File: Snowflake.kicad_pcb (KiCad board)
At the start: 2 copper layers, 168.4 x 106 mm, 34 parts, among them J1 , J2 

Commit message: updated
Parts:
- removed the ? at (217.1, 108.1)
- added ?: , Big pad, F.Cu at (237.6, 117.9)
- added ?: , Big pad, F.Cu at (224.5, 95.4)
- added ?: , Big pad, F.Cu at (235.6, 95.2)
- added ?: , Big pad, F.Cu at (222.6, 117.7)
- added ?: , Big pad, F.Cu at (243.1, 105.9)
- added ?: , Big pad, F.Cu at (222.1, 117.5)
- 2: renamed from LED5; value WS2812B -> (none)
- 4: renamed from LED3; value WS2812B -> (none)
- 5: renamed from LED2; value WS2812B -> (none)
- 6: renamed from LED104; value WS2812B -> (none)
- 7: renamed from LED101; value WS2812B -> (none)
- 8: renamed from LED102; value WS2812B -> (none)
- 9: renamed from LED103; value WS2812B -> (none)
- ?: renamed from LED7; value WS2812B -> (none)
- moved 4 2.41 mm to (124.3, 84.1)
- moved 8 1.25 mm to (123.8, 129.7)
- moved 5 1.20 mm to (109.6, 58.8)
- moved J1 0.88 mm to (230.1, 112.0)
- moved ? 0.51 mm to (217.1, 106.0)
- moved 9 0.23 mm to (109.1, 155.1)
- renumbered LED6 to 1, LED4 to 3, J2 to ?
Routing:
- net /DIN: track 66.7 -> 79.6 mm
- net /DOUT: track 179.3 -> 187.0 mm
- net /VCC: track 379.7 -> 384.3 mm, vias 22 -> 21
- net /GND: track 343.0 -> 347.2 mm
- net Net-(LED2-Pad4): track 21.6 -> 25.2 mm
- net Net-(LED3-Pad4): track 31.9 -> 29.5 mm
- net (no net): track 0.00 -> 1.97 mm, vias 0 -> 2
- net Net-(LED102-Pad2): track 23.3 -> 24.8 mm
- net Net-(LED101-Pad2): track 65.2 -> 63.9 mm
- net Net-(LED104-Pad4): track 65.9 -> 66.9 mm
- net Net-(LED6-Pad4): track 28.1 -> 29.1 mm
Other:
- board text added: "1"
- board text added: "2"
- board text added: "3"
- board text added: "4"
- board text added: "5"
- board text added: "6"
- board text added: "V0.9 Snowflake"
- board text added: "eag"

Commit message: updated
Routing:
- net (no net): track 1.97 -> 5.84 mm, vias 2 -> 3
- net /GND: track 347.2 -> 345.5 mm
- net /VCC: track 384.3 -> 385.9 mm, vias 21 -> 22
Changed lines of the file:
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@@
     (thickness 1.6)
     (drawings 92)
-    (tracks 287)
+    (tracks 293)
     (zones 0)
     (modules 39)
@@
   )
   (setup
-    (last_trace_width 0.25)
+    (last_trace_width 2)
     (user_trace_width 0.5)
     (user_trace_width 1)
@@
   (gr_line (start 139.085367 110.601745) (end 110.515198 160.077503) (layer Edge.Cuts) (width 0.1))
   (gr_line (start 131.016096 110.601745) (end 139.085367 110.601745) (layer Edge.Cuts) (width 0.1))
+  (segment (start 243.0145 105.664) (end 239.141 105.664) (width 2) (layer F.Cu) (net 0) (status 400000))
+  (via (at 239.141 105.664) (size 0.6) (drill 0.4) (layers F.Cu B.Cu) (net 0))
   (segment (start 235.290295 119.016015) (end 233.3625 118.9355) (width 2) (layer F.Cu) (net 0))
   (via (at 233.3625 118.9355) (size 0.6) (drill 0.4) (layers F.Cu B.Cu) (net 0))
@@
   (via (at 233.372871 118.953707) (size 0.6) (drill 0.4) (layers F.Cu B.Cu) (net 0))
   (segment (start 233.372871 118.953707) (end 233.3625 118.9355) (width 2) (layer F.Cu) (net 0))
+  (segment (start 239.395 98.8695) (end 240.8555 99.568) (width 2) (layer F.Cu) (net 1))
+  (via (at 240.8555 99.568) (size 0.6) (drill 0.4) (layers F.Cu B.Cu) (net 1))
+  (segment (start 240.8555 99.568) (end 240.862326 99.556012) (width 2) (layer B.Cu) (net 1))
   (segment (start 222.28403 117.711985) (end 221.361 115.951) (width 2) (layer F.Cu) (net 1))
   (via (at 221.361 115.951) (size 0.6) (drill 0.4) (layers F.Cu B.Cu) (net 1))
@@
   (segment (start 235.077 117.983) (end 241.935 114.1095) (width 2) (layer B.Cu) (net 1))
   (segment (start 241.935 114.1095) (end 241.935 108.585) (width 2) (layer B.Cu) (net 1))
-  (segment (start 241.9985 100.203) (end 239.459092 98.756948) (width 2) (layer B.Cu) (net 1))
+  (segment (start 241.9985 100.203) (end 240.862326 99.556012) (width 2) (layer B.Cu) (net 1))
+  (segment (start 240.862326 99.556012) (end 239.459092 98.756948) (width 2) (layer B.Cu) (net 1))
   (segment (start 239.459092 98.756948) (end 238.288953 98.090619) (width 2) (layer B.Cu) (net 1))
   (segment (start 238.288953 98.090619) (end 237.4265 97.5995) (width 2) (layer B.Cu) (net 1))
@@
   (segment (start 166.9415 105.41) (end 136.271 105.41) (width 2) (layer B.Cu) (net 1))
   (segment (start 136.271 105.41) (end 133.985 105.41) (width 2) (layer B.Cu) (net 1))
-  (segment (start 224.663 119.126) (end 226.633966 115.698233) (width 2) (layer B.Cu) (net 2))
-  (via (at 226.633966 115.698233) (size 0.6) (drill 0.4) (layers F.Cu B.Cu) (net 2))
-  (segment (start 226.633966 115.698233) (end 226.6315 115.697) (width 2) (layer F.Cu) (net 2))
-  (segment (start 237.70997 117.619015) (end 235.6485 114.173) (width 2) (layer F.Cu) (net 2))
-  (via (at 235.6485 114.173) (size 0.6) (drill 0.4) (layers F.Cu B.Cu) (net 2))
-  (segment (start 235.30153 95.169485) (end 233.3625 98.4885) (width 2) (layer F.Cu) (net 2))
-  (via (at 233.3625 98.4885) (size 0.6) (drill 0.4) (layers F.Cu B.Cu) (net 2))
-  (segment (start 233.3625 98.4885) (end 233.338283 98.532759) (width 2) (layer B.Cu) (net 2))
-  (segment (start 222.272795 96.537015) (end 224.409 100.1395) (width 2) (layer F.Cu) (net 2))
-  (via (at 224.409 100.1395) (size 0.6) (drill 0.4) (layers F.Cu B.Cu) (net 2))
-  (segment (start 224.409 100.1395) (end 224.189382 100.281244) (width 2) (layer B.Cu) (net 2))
-  (segment (start 243.0145 105.664) (end 238.887 105.664) (width 2) (layer F.Cu) (net 2))
-  (via (at 238.887 105.664) (size 0.6) (drill 0.4) (layers F.Cu B.Cu) (net 2))
-  (segment (start 238.887 105.664) (end 238.8235 105.664) (width 2) (layer B.Cu) (net 2))
+  (segment (start 239.2045 107.188) (end 239.141 108.6485) (width 2) (layer F.Cu) (net 2))
+  (via (at 239.141 108.6485) (size 0.6) (drill 0.4) (layers F.Cu B.Cu) (net 2))
+  (segment (start 235.458 107.188) (end 239.2045 107.188) (width 2) (layer F.Cu) (net 2) (status 400000))
+  (via (at 239.2045 107.188) (size 0.6) (drill 0.4) (layers F.Cu B.Cu) (net 2))
+  (segment (start 239.2045 107.188) (end 239.141 107.188) (width 2) (layer B.Cu) (net 2))
+  (segment (start 224.663 119.126) (end 226.6315 115.697) (width 2) (layer B.Cu) (net 2))
+  (via (at 226.6315 115.697) (size 0.6) (drill 0.4) (layers F.Cu B.Cu) (net 2))
+  (segment (start 226.6315 115.697) (end 226.629034 115.695767) (width 2) (layer F.Cu) (net 2))
+  (segment (start 237.70997 117.619015) (end 236.0295 114.173) (width 2) (layer F.Cu) (net 2) (status 400000))
+  (via (at 236.0295 114.173) (size 0.6) (drill 0.4) (layers F.Cu B.Cu) (net 2))
+  (segment (start 235.30153 95.169485) (end 233.553 98.425) (width 2) (layer F.Cu) (net 2) (status 400000))
+  (via (at 233.553 98.425) (size 0.6) (drill 0.4) (layers F.Cu B.Cu) (net 2))
+  (segment (start 233.553 98.425) (end 233.528783 98.469259) (width 2) (layer B.Cu) (net 2))
+  (segment (start 222.272795 96.537015) (end 224.282 99.822) (width 2) (layer F.Cu) (net 2) (status 400000))
+  (via (at 224.282 99.822) (size 0.6) (drill 0.4) (layers F.Cu B.Cu) (net 2))
+  (segment (start 224.282 99.822) (end 224.062382 99.963744) (width 2) (layer B.Cu) (net 2))
   (via (at 213.614 108.5215) (size 0.6) (drill 0.4) (layers F.Cu B.Cu) (net 2))
   (segment (start 213.614 108.5215) (end 216.9795 108.5215) (width 2) (layer F.Cu) (net 2))
@@
   (segment (start 211.2645 107.95) (end 213.614 108.5215) (width 2) (layer B.Cu) (net 2))
   (segment (start 220.98 108.3945) (end 220.98 108.0135) (width 2) (layer B.Cu) (net 2))
-  (segment (start 226.6315 115.697) (end 227.3935 116.078) (width 2) (layer B.Cu) (net 2))
+  (segment (start 226.629034 115.695767) (end 227.391034 116.076767) (width 2) (layer B.Cu) (net 2))
   (segment (start 173.85 108.457) (end 175.7045 108.1405) (width 1) (layer F.Cu) (net 2))
   (via (at 175.7045 108.1405) (size 0.6) (drill 0.4) (layers F.Cu B.Cu) (net 2))
@@
   (segment (start 131.495605 99.590527) (end 131.3815 103.5685) (width 2) (layer F.Cu) (net 2))
   (segment (start 131.3815 103.5685) (end 131.38138 108.188374) (width 2) (layer F.Cu) (net 2))
-  (segment (start 227.3935 116.078) (end 227.401315 116.064323) (width 2) (layer B.Cu) (net 2))
+  (segment (start 227.391034 116.076767) (end 227.398849 116.06309) (width 2) (layer B.Cu) (net 2))
   (segment (start 134.493 107.95) (end 134.492778 108.052098) (width 2) (layer B.Cu) (net 2))
   (via (at 134.493 107.95) (size 0.6) (drill 0.4) (layers F.Cu B.Cu) (net 2))
@@
   (segment (start 235.458 107.188) (end 233.426 107.188) (width 1) (layer F.Cu) (net 2))
   (segment (start 233.426 107.188) (end 232.27 108.33) (width 1) (layer F.Cu) (net 2))
-  (segment (start 235.458 107.188) (end 238.76 107.188) (width 2) (layer F.Cu) (net 2))
-  (via (at 238.76 107.188) (size 0.6) (drill 0.4) (layers F.Cu B.Cu) (net 2))
-  (segment (start 220.98 102.235) (end 224.570382 100.090744) (width 2) (layer B.Cu) (net 2))
-  (segment (start 224.570382 100.090744) (end 230.124 96.774) (width 2) (layer B.Cu) (net 2))
+  (segment (start 220.98 101.727) (end 224.443382 99.773244) (width 2) (layer B.Cu) (net 2))
+  (segment (start 224.443382 99.773244) (end 230.1875 96.5835) (width 2) (layer B.Cu) (net 2))
   (segment (start 220.98 112.395) (end 220.98 108.0135) (width 2) (layer B.Cu) (net 2))
-  (segment (start 220.98 108.0135) (end 220.98 102.235) (width 2) (layer B.Cu) (net 2))
-  (segment (start 229.87 117.475) (end 227.401315 116.064323) (width 2) (layer B.Cu) (net 2))
-  (segment (start 227.401315 116.064323) (end 220.98 112.395) (width 2) (layer B.Cu) (net 2))
-  (segment (start 238.76 112.395) (end 235.6485 114.173) (width 2) (layer B.Cu) (net 2))
-  (segment (start 235.6485 114.173) (end 229.87 117.475) (width 2) (layer B.Cu) (net 2))
-  (segment (start 238.76 101.6) (end 238.8235 105.664) (width 2) (layer B.Cu) (net 2))
-  (segment (start 238.8235 105.664) (end 238.8235 106.3625) (width 2) (layer B.Cu) (net 2))
-  (segment (start 238.8235 106.3625) (end 238.76 107.188) (width 2) (layer B.Cu) (net 2))
-  (segment (start 238.76 107.188) (end 238.76 112.395) (width 2) (layer B.Cu) (net 2))
-  (segment (start 230.124 96.774) (end 233.338283 98.532759) (width 2) (layer B.Cu) (net 2))
-  (segment (start 233.338283 98.532759) (end 233.4895 98.6155) (width 2) (layer B.Cu) (net 2))
-  (segment (start 233.4895 98.6155) (end 233.619012 98.687874) (width 2) (layer B.Cu) (net 2))
-  (segment (start 233.619012 98.687874) (end 238.76 101.6) (width 2) (layer B.Cu) (net 2))
+  (segment (start 220.98 108.0135) (end 220.98 101.727) (width 2) (layer B.Cu) (net 2))
+  (segment (start 230.124 117.602) (end 227.398849 116.06309) (width 2) (layer B.Cu) (net 2))
+  (segment (start 227.398849 116.06309) (end 220.98 112.395) (width 2) (layer B.Cu) (net 2))
+  (segment (start 239.141 112.395) (end 236.0295 114.173) (width 2) (layer B.Cu) (net 2))
+  (segment (start 236.0295 114.173) (end 230.124 117.602) (width 2) (layer B.Cu) (net 2))
+  (segment (start 239.141 101.7905) (end 239.141 105.664) (width 2) (layer B.Cu) (net 2))
+  (segment (start 239.141 105.664) (end 239.141 107.188) (width 2) (layer B.Cu) (net 2))
+  (segment (start 239.141 107.188) (end 239.141 108.6485) (width 2) (layer B.Cu) (net 2))
+  (segment (start 239.141 108.6485) (end 239.141 112.395) (width 2) (layer B.Cu) (net 2))
+  (segment (start 230.1875 96.5835) (end 233.528783 98.469259) (width 2) (layer B.Cu) (net 2))
+  (segment (start 233.528783 98.469259) (end 233.68 98.552) (width 2) (layer B.Cu) (net 2))
+  (segment (start 233.68 98.552) (end 233.809512 98.624374) (width 2) (layer B.Cu) (net 2))
+  (segment (start 233.809512 98.624374) (end 239.141 101.7905) (width 2) (layer B.Cu) (net 2))
   (segment (start 203.06 108.33) (end 205.486 107.95) (width 1) (layer F.Cu) (net 2))
   (via (at 205.486 107.95) (size 0.6) (drill 0.4) (layers F.Cu B.Cu) (net 2))

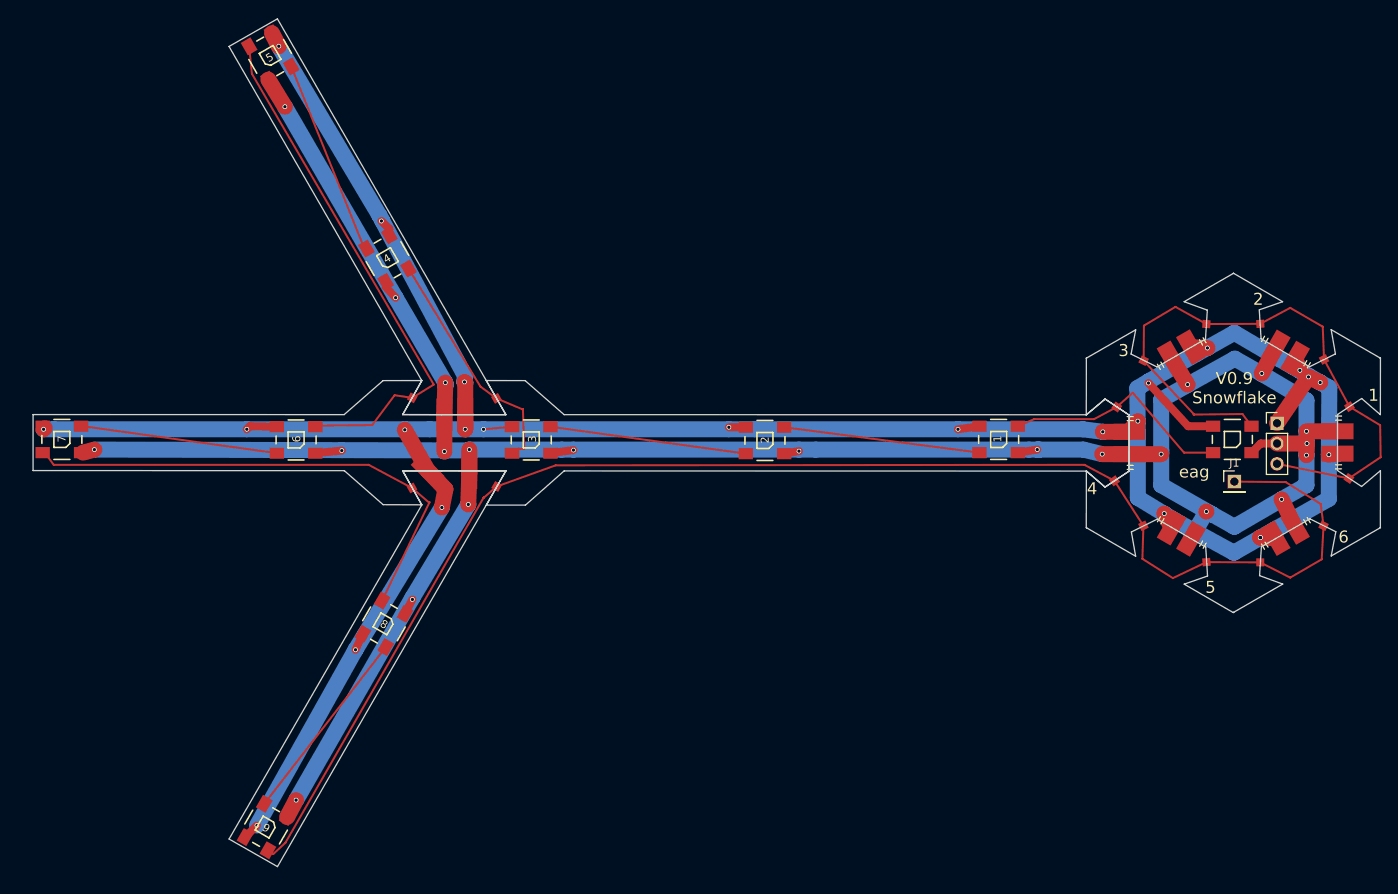
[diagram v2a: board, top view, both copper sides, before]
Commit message: New small pads
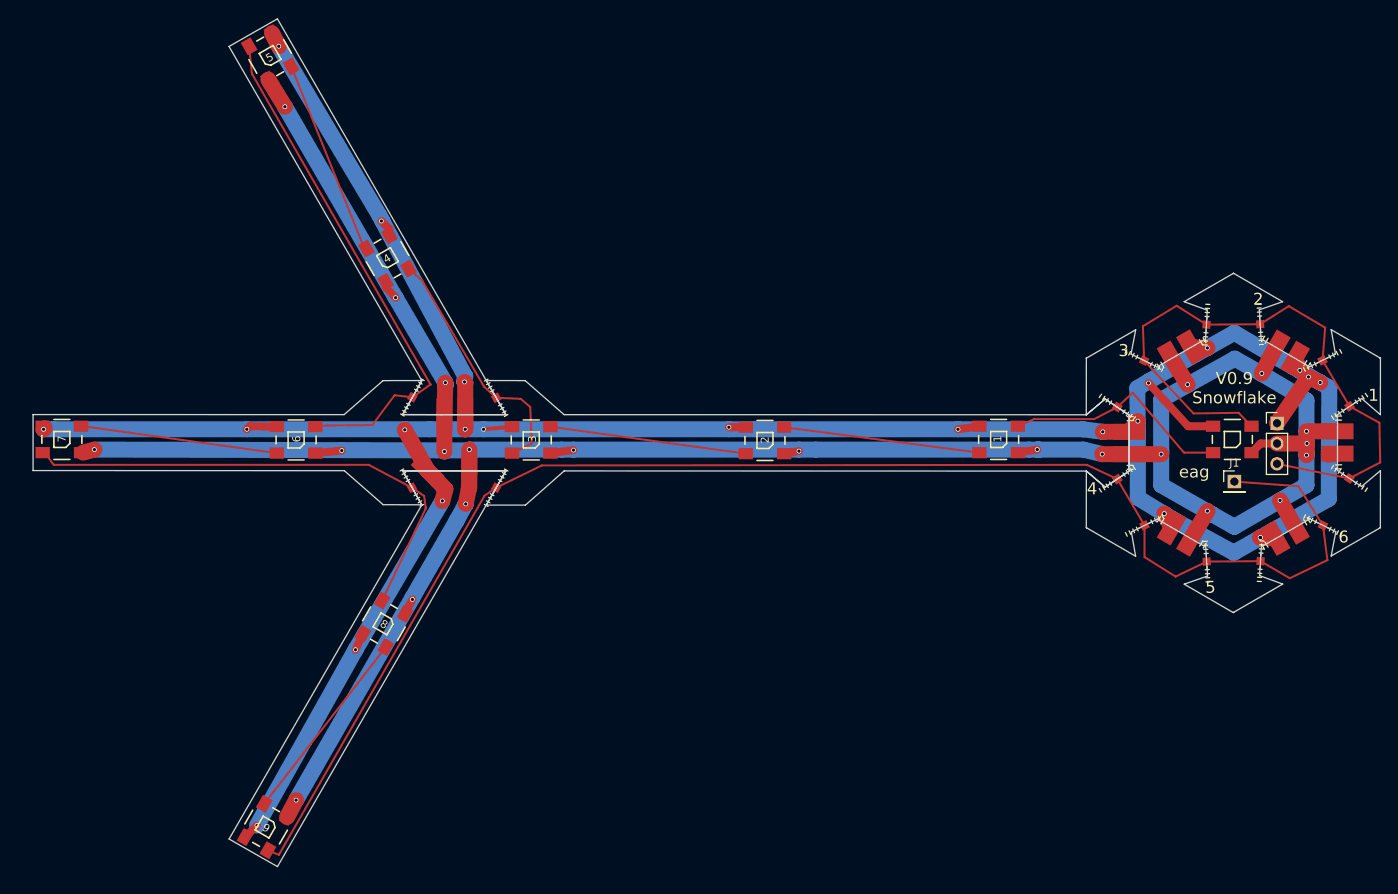
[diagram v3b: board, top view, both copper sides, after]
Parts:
- removed the ? at (239.5, 123.7)
- removed the ? at (221.0, 109.6)
- removed the ? at (234.6, 86.0)
- removed the ? at (224.6, 98.2)
- removed the ? at (214.1, 92.6)
- removed the ? at (219.6, 107.4)
- removed the ? at (136.3, 95.4)
- removed the ? at (128.8, 118.9)
- removed the ? at (142.4, 108.1)
- removed the ? at (225.0, 116.4)
- removed the ? at (232.9, 123.1)
- removed the ? at (246.0, 121.7)
- removed the ? at (240.3, 106.8)
- removed the ? at (250.5, 100.6)
- removed the ? at (235.1, 97.9)
- added ?: , Tiny Edge, F.Cu at (215.5, 111.6)
- added ?: , Tiny Edge, F.Cu at (226.6, 92.3)
- added ?: , Tiny Edge, F.Cu at (218.8, 96.8)
- added ?: , Tiny Edge, F.Cu at (215.5, 102.6)
- added ?: , Tiny Edge, F.Cu at (137.9, 101.5)
- added ?: , Tiny Edge, F.Cu at (127.3, 112.7)
- added ?: , Tiny Edge, F.Cu at (137.9, 112.7)
- added ?: , Tiny Edge, F.Cu at (218.9, 117.4)
- added ?: , Tiny Edge, F.Cu at (226.7, 121.9)
- added ?: , Tiny Edge, F.Cu at (233.4, 121.9)
- added ?: , Tiny Edge, F.Cu at (241.2, 117.4)
- added ?: , Tiny Edge, F.Cu at (244.5, 111.6)
- added ?: , Tiny Edge, F.Cu at (244.5, 102.5)
- added ?: , Tiny Edge, F.Cu at (241.1, 96.8)
- added ?: , Tiny Edge, F.Cu at (233.3, 92.3)
- moved ? 6.38 mm to (127.4, 101.4)
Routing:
- net /GND: track 345.5 -> 349.4 mm, vias 21 -> 22
- net (no net): track 5.84 -> 3.06 mm, vias 3 -> 2
- net /VCC: track 385.9 -> 383.6 mm, vias 22 -> 21
- net Net-(LED3-Pad4): track 29.5 -> 31.6 mm
- net /DIN: track 79.6 -> 80.4 mm
- net /DOUT: track 187.0 -> 187.6 mm
- net Net-(LED104-Pad4): track 66.9 -> 66.3 mm

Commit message: updated
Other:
- board text added: "+"
- board text added: "-"
- board text added: "G"
- board text added: "GND"
- board text added: "V"
- board text added: "VCC"
- board text added: "d"
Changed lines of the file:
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@@
     (links 31)
     (no_connects 0)
-    (area 79.915196 54.05732 251.591687 160.127504)
+    (area 79.915196 54.05732 248.686202 160.127504)
     (thickness 1.6)
-    (drawings 92)
+    (drawings 103)
     (tracks 293)
     (zones 0)
@@
     (pad_to_mask_clearance 0.2)
     (aux_axis_origin 0 0)
-    (visible_elements 7FFFFFFF)
+    (visible_elements 7FFFF7FF)
     (pcbplotparams
       (layerselection 0x00030_80000001)
@@
     )
   )
+  (gr_text G (at 129.7432 96.774) (layer F.SilkS)
+    (effects (font (size 1.5 1.5) (thickness 0.3)))
+  )
+  (gr_text V (at 132.2832 96.0628) (layer F.SilkS)
+    (effects (font (size 1.5 1.5) (thickness 0.3)))
+  )
+  (gr_text G (at 132.2578 117.6274) (layer F.SilkS)
+    (effects (font (size 1.5 1.5) (thickness 0.3)))
+  )
+  (gr_text V (at 129.6162 117.475) (layer F.SilkS)
+    (effects (font (size 1.5 1.5) (thickness 0.3)))
+  )
+  (gr_text d (at 237.49 109.5756) (layer F.SilkS)
+    (effects (font (size 1.5 1.5) (thickness 0.3)))
+  )
+  (gr_text - (at 237.7186 106.9848) (layer F.SilkS)
+    (effects (font (size 1.5 1.5) (thickness 0.3)))
+  )
+  (gr_text + (at 237.5662 104.4702) (layer F.SilkS)
+    (effects (font (size 1.5 1.5) (thickness 0.3)))
+  )
+  (gr_text G (at 229.9462 117.6274) (layer F.SilkS)
+    (effects (font (size 1.5 1.5) (thickness 0.3)))
+  )
+  (gr_text V (at 230.0478 120.777) (layer F.SilkS)
+    (effects (font (size 1.5 1.5) (thickness 0.3)))
+  )
+  (gr_text GND (at 208.5848 108.0262) (layer F.SilkS)
+    (effects (font (size 1.5 1.5) (thickness 0.3)))
+  )
+  (gr_text VCC (at 208.534 105.537) (layer F.SilkS)
+    (effects (font (size 1.5 1.5) (thickness 0.3)))
+  )
   (gr_text eag (at 225.1075 110.744) (layer F.SilkS)

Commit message: changes, added esp controller
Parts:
- added ?: , Tiny Edge, F.Cu at (215.2, 103.1)
- added ?: , Tiny Edge, F.Cu at (215.8, 112.0)
- added ?: , Tiny Edge, F.Cu at (138.3, 113.0)
- added ?: , Tiny Edge, F.Cu at (127.0, 113.0)
- added ?: , Tiny Edge, F.Cu at (127.8, 101.7)
- added ?: , Tiny Edge, F.Cu at (138.3, 101.2)
- moved ? 0.53 mm to (127.8, 112.5)
- moved ? 0.52 mm to (232.9, 121.9)
- moved ? 0.51 mm to (215.2, 111.2)
- moved ? 0.50 mm to (137.4, 101.7)
- moved ? 0.50 mm to (241.4, 97.2)
- moved ? 0.50 mm to (218.7, 97.3)
- moved ? 0.49 mm to (126.9, 101.2)
- moved ? 0.49 mm to (215.8, 102.2)
- moved ? 0.49 mm to (137.4, 112.5)
- moved ? 0.48 mm to (244.3, 112.0)
- moved ? 0.48 mm to (227.1, 92.4)
- moved ? 0.48 mm to (241.4, 117.0)
- moved ? 0.47 mm to (232.9, 92.3)
- moved ? 0.47 mm to (227.1, 121.9)
- moved ? 0.47 mm to (244.3, 102.1)
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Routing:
- net (no net): track 3.06 -> 44.8 mm
- net /DOUT: track 187.6 -> 148.1 mm
- net /DIN: track 80.4 -> 82.7 mm
- net Net-(LED101-Pad2): track 63.7 -> 61.5 mm
- net /VCC: track 383.6 -> 384.7 mm, vias 21 -> 22
- net Net-(LED3-Pad4): track 31.6 -> 32.3 mm
- net Net-(LED104-Pad4): track 66.3 -> 66.8 mm
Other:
- board text added: "V1.0 Snowflake"
- board text removed: "V0.9 Snowflake"
